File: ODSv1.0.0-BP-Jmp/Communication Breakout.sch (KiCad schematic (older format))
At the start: 2 parts, among them J10 Conn_02x10_Odd_Even, J11 Conn_02x10_Odd_Even

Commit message: Fix hierarchical pin label directions, finish front right corner
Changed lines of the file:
@@
 Comment4 ""
 $EndDescr
-Text HLabel 2250 1900 2    50   Input ~ 0
+Text HLabel 2250 1900 2    50   Output ~ 0
 SER3_RX
-Text HLabel 2250 1800 2    50   Output ~ 0
+Text HLabel 2250 1800 2    50   Input ~ 0
 SER3_TX
-Text HLabel 2250 1300 2    50   Input ~ 0
+Text HLabel 2250 1300 2    50   Output ~ 0
 SER7_RX
-Text HLabel 2250 1200 2    50   Output ~ 0
+Text HLabel 2250 1200 2    50   Input ~ 0
 SER7_TX
-Text HLabel 2250 1700 2    50   Input ~ 0
+Text HLabel 2250 1700 2    50   Output ~ 0
 SER2_RX
-Text HLabel 2250 1600 2    50   Output ~ 0
+Text HLabel 2250 1600 2    50   Input ~ 0
 SER2_TX
-Text HLabel 2250 1100 2    50   Input ~ 0
+Text HLabel 2250 1100 2    50   Output ~ 0
 SER8_RX
-Text HLabel 2250 1000 2    50   Output ~ 0
+Text HLabel 2250 1000 2    50   Input ~ 0
 SER8_TX
-Text HLabel 2250 1500 2    50   Input ~ 0
+Text HLabel 2250 1500 2    50   Output ~ 0
 CAN2_CRX
-Text HLabel 2250 1400 2    50   Output ~ 0
+Text HLabel 2250 1400 2    50   Input ~ 0
 CAN2_CTX
 Text HLabel 2250 3400 2    50   BiDi ~ 0
 I2C2_SDA
-Text HLabel 2250 3300 2    50   Output ~ 0
+Text HLabel 2250 3300 2    50   Input ~ 0
 I2C2_SCL
 Text HLabel 2250 3200 2    50   BiDi ~ 0
 I2C1_SDA
-Text HLabel 2250 3100 2    50   Output ~ 0
+Text HLabel 2250 3100 2    50   Input ~ 0
 I2C1_SCL
 Text HLabel 2250 2600 2    50   BiDi ~ 0
 I2C0_SDA
-Text HLabel 2250 2500 2    50   Output ~ 0
+Text HLabel 2250 2500 2    50   Input ~ 0
 I2C0_SCL
 $Comp
@@
 Text HLabel 2250 2800 2    50   BiDi ~ 0
 I2C0_SDA
-Text HLabel 2250 2700 2    50   Output ~ 0
+Text HLabel 2250 2700 2    50   Input ~ 0
 I2C0_SCL
 Text HLabel 2250 3000 2    50   BiDi ~ 0
 I2C0_SDA
-Text HLabel 2250 2900 2    50   Output ~ 0
+Text HLabel 2250 2900 2    50   Input ~ 0
 I2C0_SCL
 Wire Wire Line

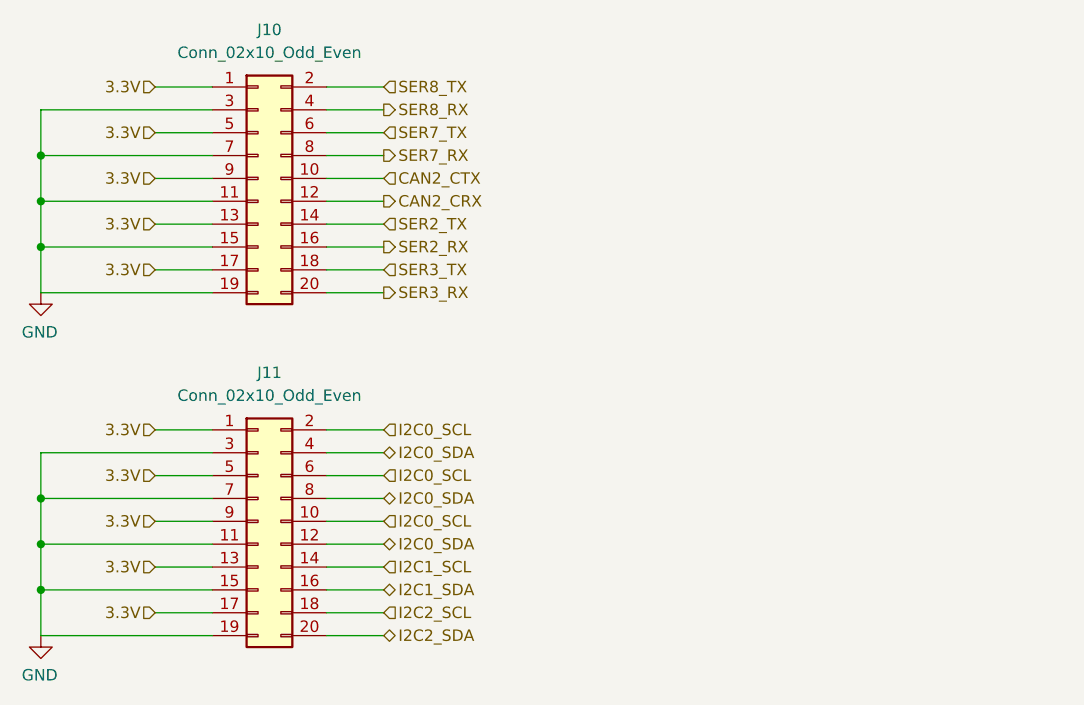
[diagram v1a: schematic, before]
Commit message: Finish rear right corner
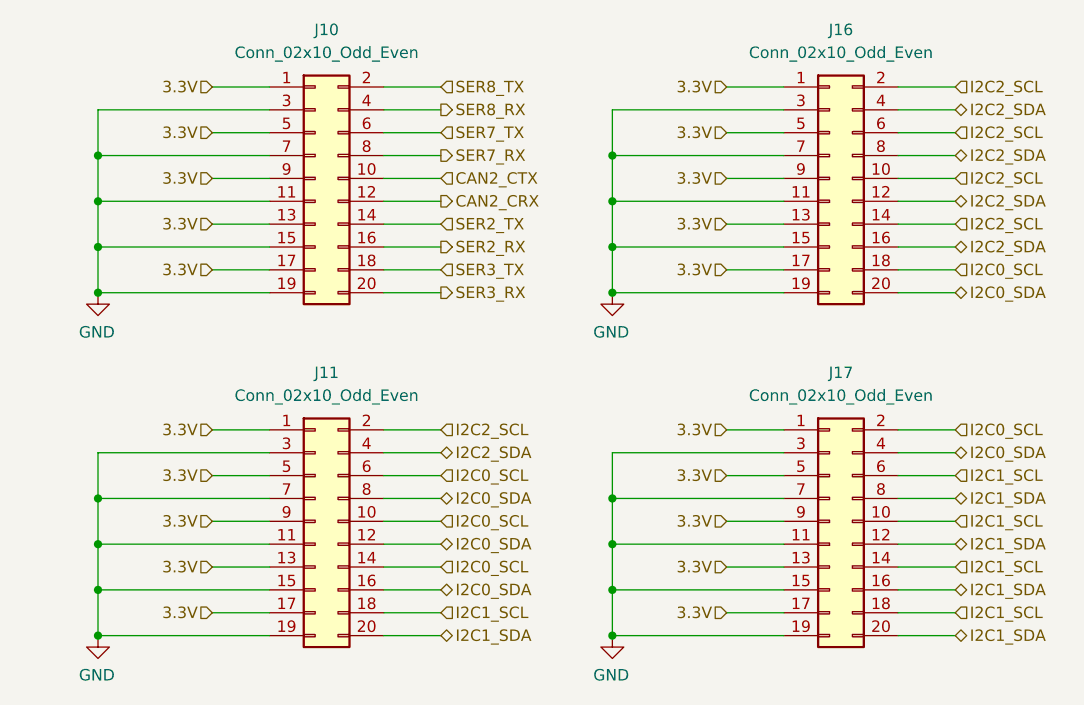
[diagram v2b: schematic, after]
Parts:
- added J16, J17: Conn_02x10_Odd_Even, Connector_PinHeader_2.54mm:PinHeader_2x10_P2.54mm_Vertical_SMD, symbol Connector_Generic:Conn_02x10_Odd_Even
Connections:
- net 3.3V: now also J16.1 (Pin_1), J16.13 (Pin_13), J16.17 (Pin_17), J16.5 (Pin_5), J16.9 (Pin_9), J17.1 (Pin_1), J17.13 (Pin_13), J17.17 (Pin_17), J17.5 (Pin_5), J17.9 (Pin_9)
- net GND: now also J16.11 (Pin_11), J16.15 (Pin_15), J16.19 (Pin_19), J16.3 (Pin_3), J16.7 (Pin_7), J17.11 (Pin_11), J17.15 (Pin_15), J17.19 (Pin_19), J17.3 (Pin_3), J17.7 (Pin_7)
- net I2C0_SCL: now also J11.14 (Pin_14), J16.18 (Pin_18), J17.2 (Pin_2); no longer J11.2 (Pin_2)
- net I2C0_SDA: now also J11.16 (Pin_16), J16.20 (Pin_20), J17.4 (Pin_4); no longer J11.4 (Pin_4)
- net I2C1_SCL: now also J11.18 (Pin_18), J17.10 (Pin_10), J17.14 (Pin_14), J17.18 (Pin_18), J17.6 (Pin_6); no longer J11.14 (Pin_14)
- net I2C1_SDA: now also J11.20 (Pin_20), J17.12 (Pin_12), J17.16 (Pin_16), J17.20 (Pin_20), J17.8 (Pin_8); no longer J11.16 (Pin_16)
- net I2C2_SCL: now also J11.2 (Pin_2), J16.10 (Pin_10), J16.14 (Pin_14), J16.2 (Pin_2), J16.6 (Pin_6); no longer J11.18 (Pin_18)
- net I2C2_SDA: now also J11.4 (Pin_4), J16.12 (Pin_12), J16.16 (Pin_16), J16.4 (Pin_4), J16.8 (Pin_8); no longer J11.20 (Pin_20)
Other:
- moved on the sheet: J10, J11
